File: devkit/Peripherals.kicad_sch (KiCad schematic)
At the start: 46 parts, among them IC501 APDS-9306-065, IC502 BMI270, IC503 LIS2MDLTR, IC504 BMP581, IC505 DRV2603RUNT, IC506 PCA9306JK, IC507 RV-8263-C8, J501 Jumper, J502 Jumper, J503 Jumper, J504 Jumper, J505 Jumper, J506 Jumper, J507 Jumper, M501 Vibrator DC Motor, X501 Current, X502 I2S, X503 Current, X504 I2C, X505 Current, X506 Current, X507 Current, X508 Current, X509 Motor, X510 Current

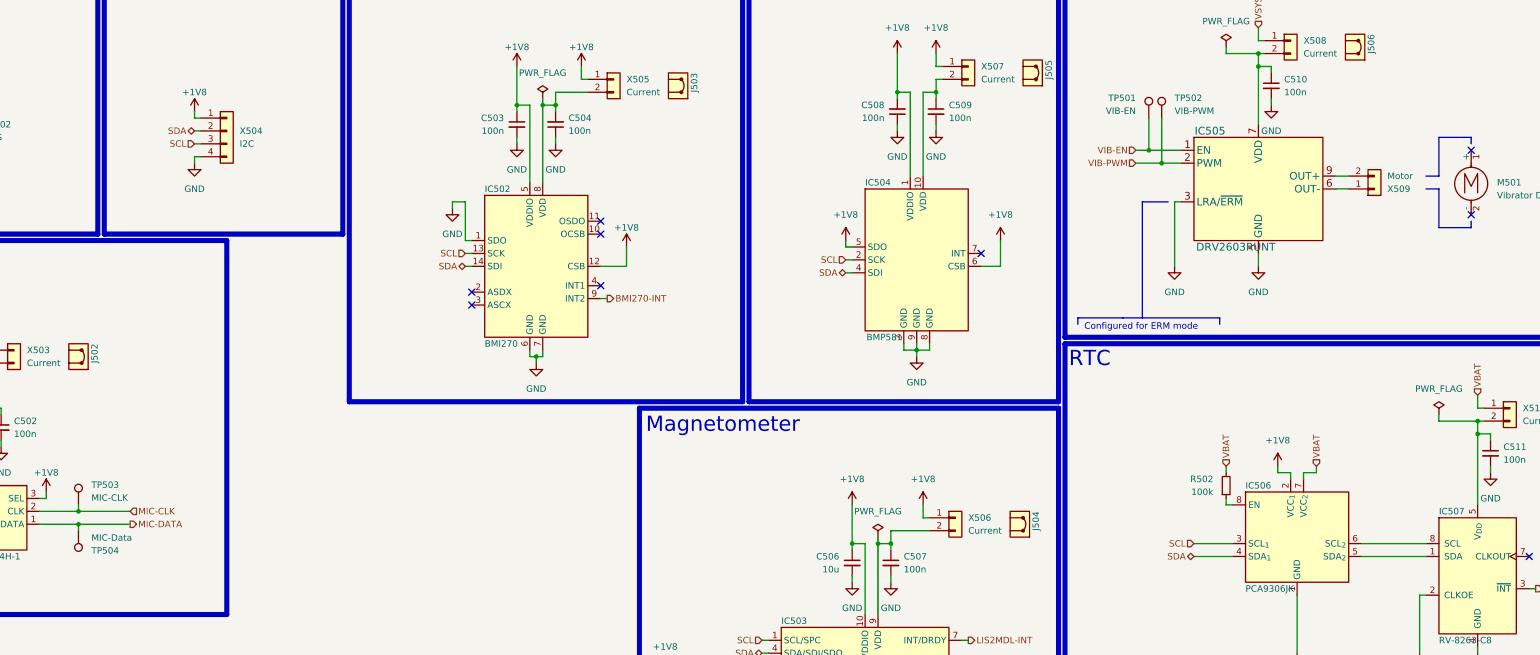
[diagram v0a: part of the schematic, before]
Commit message: Bug: Issue #158
- Fix silkscreens
- Add pull-up resistors to I2C lines
- Set the Pull-Up for Flash CS to NA
- Fix wrong part number for the I2C header

Closes #158

Signed-off-by: Daniel Kampert <DanielKampert@kampis-elektroecke.de>
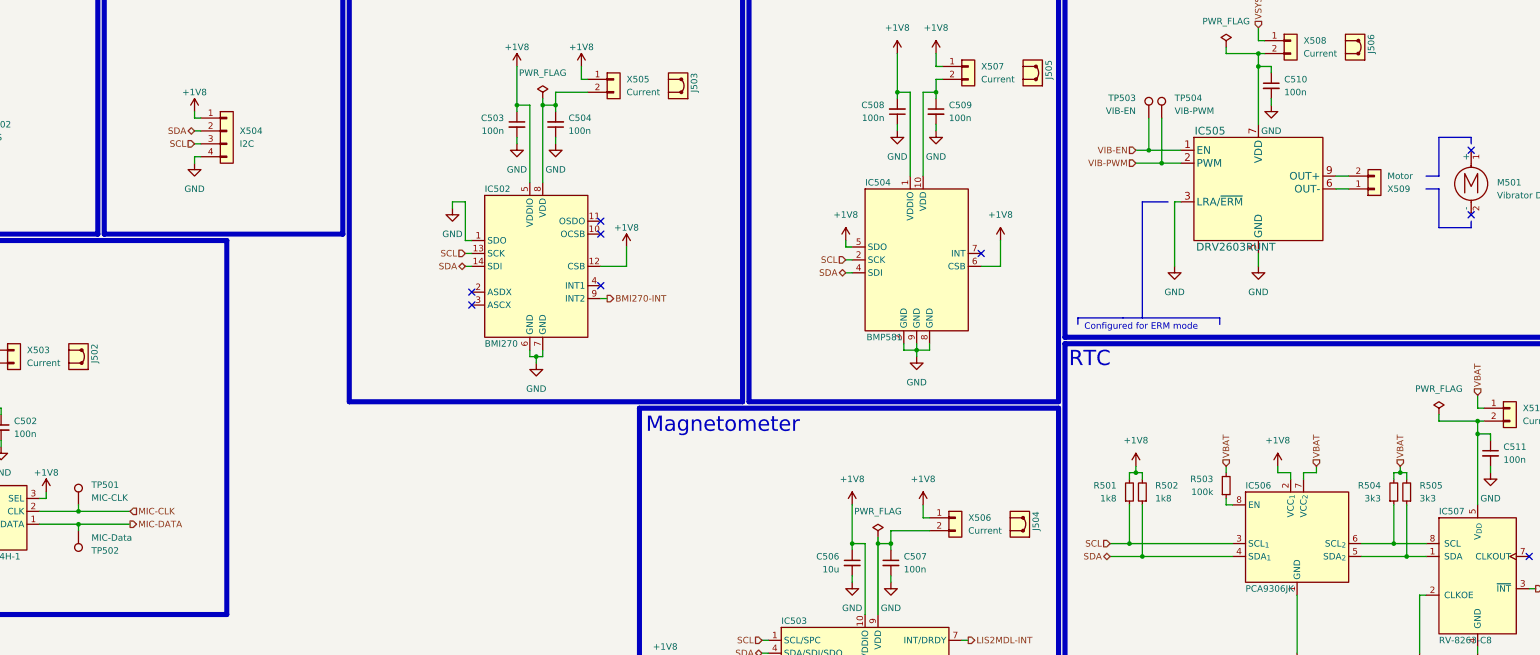
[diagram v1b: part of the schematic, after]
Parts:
- added R501, R502: 1k8, Resistor_SMD:R_0402_1005Metric, symbol Device:R_Small
- added R504, R505: 3k3, Resistor_SMD:R_0402_1005Metric, symbol Device:R_Small
- X504: manf# 77311-818-02LF -> 77311-818-04LF; mouser# 649-77311-818-02LF -> 649-77311-818-04LF
- renumbered R502 to R503, TP503 to TP501, TP504 to TP502, TP501 to TP503, TP502 to TP504
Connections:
- net +1V8: now also R501.2, R502.2
- net SCL: now also R501.1
- net SDA: now also R502.1
- net VBAT: now also R504.2, R505.2
- net at IC506.5 (SDA_{2}), IC507.1 (SDA): now also R505.1
- net at IC506.6 (SCL_{2}), IC507.8 (SCL): now also R504.1

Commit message: Release 1.2.1
Signed-off-by: Daniel Kampert <DanielKampert@kampis-elektroecke.de>
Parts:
- R501, R502: manf# RC0404FR-071K8L -> RC0402FR-071K8L; mouser# 603-RC0404FR-071K8L -> 603-RC0402FR-071K8L
- R503: manf# RC0404FR-07100KL -> RC0402FR-07100KL; mouser# 603-RC0404FR-07100KL -> 603-RC0402FR-07100KL
- R504, R505: manf# RC0404FR-073K3L -> RC0402FR-073K3L; mouser# 603-RC0404FR-073K3L -> 603-RC0402FR-073K3L
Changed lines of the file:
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@@
 			)
 		)
-		(property "manf#" "RC0404FR-073K3L"
+		(property "manf#" "RC0402FR-073K3L"
 			(at 364.49 121.92 0)
 			(effects
@@
 			)
 		)
-		(property "mouser#" "603-RC0404FR-073K3L"
+		(property "mouser#" "603-RC0402FR-073K3L"
 			(at 364.49 121.92 0)
 			(effects
@@
 			)
 		)
-		(property "manf#" "RC0404FR-071K8L"
+		(property "manf#" "RC0402FR-071K8L"
 			(at 314.96 121.92 0)
 			(effects
@@
 			)
 		)
-		(property "mouser#" "603-RC0404FR-071K8L"
+		(property "mouser#" "603-RC0402FR-071K8L"
 			(at 314.96 121.92 0)
 			(effects
@@
 			)
 		)
-		(property "manf#" "RC0404FR-07100KL"
+		(property "manf#" "RC0402FR-07100KL"
 			(at 331.47 120.65 0)
 			(effects
@@
 			)
 		)
-		(property "mouser#" "603-RC0404FR-07100KL"
+		(property "mouser#" "603-RC0402FR-07100KL"
 			(at 331.47 120.65 0)
 			(effects
@@
 			)
 		)
-		(property "manf#" "RC0404FR-073K3L"
+		(property "manf#" "RC0402FR-073K3L"
 			(at 367.03 121.92 0)
 			(effects
@@
 			)
 		)
-		(property "mouser#" "603-RC0404FR-073K3L"
+		(property "mouser#" "603-RC0402FR-073K3L"
 			(at 367.03 121.92 0)
 			(effects
@@
 			)
 		)
-		(property "manf#" "RC0404FR-071K8L"
+		(property "manf#" "RC0402FR-071K8L"
 			(at 312.42 121.92 0)
 			(effects
@@
 			)
 		)
-		(property "mouser#" "603-RC0404FR-071K8L"
+		(property "mouser#" "603-RC0402FR-071K8L"
 			(at 312.42 121.92 0)
 			(effects

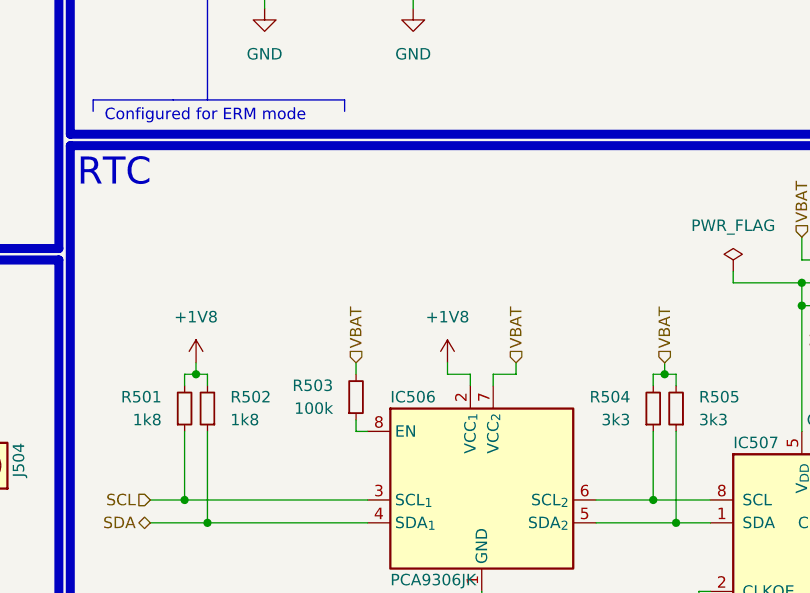
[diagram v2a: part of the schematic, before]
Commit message: Bug: Issue #172
- Fix wrong resistor for VREF2 pin for the level shifter
- Update changelog

Closes #172

Signed-off-by: Daniel Kampert <DanielKampert@kampis-elektroecke.de>
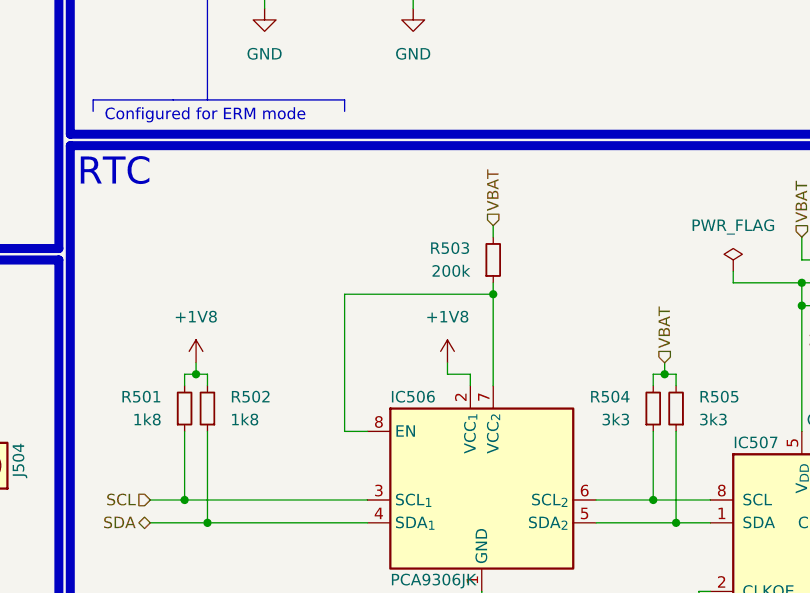
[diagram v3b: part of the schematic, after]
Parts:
- R503: value 100k -> 200k; manf# RC0402FR-07100KL -> RC0402FR-07200KL; mouser# 603-RC0402FR-07100KL -> 603-RC0402FR-07200KL
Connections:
- net VBAT: no longer IC506.7 (VCC_{2})
- net at IC506.8 (EN), R503.1: now also IC506.7 (VCC_{2})
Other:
- moved on the sheet: R503
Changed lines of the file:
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@@
 	)
 	(junction
+		(at 346.71 109.22)
+		(diameter 0)
+		(color 0 0 0 0)
+	)
+	(junction
 		(at 19.05 111.76)
 		(diameter 0)
@@
 	(wire
 		(pts
-			(xy 331.47 123.19) (xy 331.47 124.46)
+			(xy 346.71 107.95) (xy 346.71 109.22)
 		)
 		(stroke
@@
 	(wire
 		(pts
-			(xy 331.47 116.84) (xy 331.47 118.11)
+			(xy 346.71 101.6) (xy 346.71 102.87)
 		)
 		(stroke
@@
 	(wire
 		(pts
-			(xy 349.25 116.84) (xy 349.25 118.11)
-		)
-		(stroke
-			(width 0)
-			(type default)
-		)
-	)
-	(wire
-		(pts
 			(xy 199.39 43.18) (xy 199.39 45.72)
 		)
@@
 	(wire
 		(pts
+			(xy 330.2 109.22) (xy 346.71 109.22)
+		)
+		(stroke
+			(width 0)
+			(type default)
+		)
+	)
+	(wire
+		(pts
 			(xy 196.85 93.98) (xy 196.85 95.25)
 		)
@@
 	(wire
 		(pts
-			(xy 331.47 124.46) (xy 332.74 124.46)
+			(xy 330.2 124.46) (xy 332.74 124.46)
 		)
 		(stroke
@@
 	(wire
 		(pts
-			(xy 346.71 118.11) (xy 346.71 119.38)
+			(xy 346.71 109.22) (xy 346.71 119.38)
 		)
 		(stroke
@@
 	(wire
 		(pts
+			(xy 330.2 109.22) (xy 330.2 124.46)
+		)
+		(stroke
+			(width 0)
+			(type default)
+		)
+	)
+	(wire
+		(pts
 			(xy 313.69 118.11) (xy 313.69 116.84)
 		)
@@
 	(wire
 		(pts
-			(xy 349.25 118.11) (xy 346.71 118.11)
-		)
-		(stroke
-			(width 0)
-			(type default)
-		)
-	)
-	(wire
-		(pts
 			(xy 364.49 132.08) (xy 370.84 132.08)
 		)
@@
 		)
 	)
-	(hierarchical_label "VBAT"
-		(shape input)
-		(at 349.25 116.84 90)
-		(effects
-			(font
-				(size 1.27 1.27)
-			)
-			(justify left)
-		)
-	)
 	(hierarchical_label "SDA"
 		(shape bidirectional)
@@
 	(hierarchical_label "VBAT"
 		(shape input)
-		(at 331.47 116.84 90)
+		(at 346.71 101.6 90)
 		(effects
 			(font
@@
 	(symbol
 		(lib_id "Device:R_Small")
-		(at 331.47 120.65 0)
+		(at 346.71 105.41 0)
 		(mirror x)
 		(unit 1)
@@
 		(fields_autoplaced yes)
 		(property "Reference" "R503"
-			(at 328.93 119.38 0)
+			(at 344.17 104.14 0)
 			(effects
 				(font
@@
 			)
 		)
-		(property "Value" "100k"
-			(at 328.93 121.92 0)
+		(property "Value" "200k"
+			(at 344.17 106.68 0)
 			(effects
 				(font
@@
 		)
 		(property "Footprint" "Resistor_SMD:R_0402_1005Metric"
-			(at 331.47 120.65 0)
+			(at 346.71 105.41 0)
 			(effects
 				(font
@@
 		)
 		(property "Datasheet" "https://www.mouser.com/catalog/specsheets/YAGEO_PYu_RC_Group_51_RoHS_L_12.pdf"
-			(at 331.47 120.65 0)
+			(at 346.71 105.41 0)
 			(effects
 				(font
@@
 		)
 		(property "Description" "Resistor, small symbol"
-			(at 331.47 120.65 0)
+			(at 346.71 105.41 0)
 			(effects
 				(font
@@
 		)
 		(property "CONFIG" ""
-			(at 331.47 120.65 0)
+			(at 346.71 105.41 0)
 			(effects
 				(font
@@
 		)
 		(property "manf" "YAGEO"
-			(at 331.47 120.65 0)
+			(at 346.71 105.41 0)
 			(effects
 				(font
@@
 			)
 		)
-		(property "manf#" "RC0402FR-07100KL"
-			(at 331.47 120.65 0)
+		(property "manf#" "RC0402FR-07200KL"
+			(at 346.71 105.41 0)
 			(effects
 				(font
@@
 			)
 		)
-		(property "mouser#" "603-RC0402FR-07100KL"
-			(at 331.47 120.65 0)
+		(property "mouser#" "603-RC0402FR-07200KL"
+			(at 346.71 105.41 0)
 			(effects
 				(font

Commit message: Revert "Bug: Issue #172"
This reverts commit d2b21792fba04b32ee89f1631bab4de80096e44a.
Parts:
- R503: value 200k -> 100k; manf# RC0402FR-07200KL -> RC0402FR-07100KL; mouser# 603-RC0402FR-07200KL -> 603-RC0402FR-07100KL
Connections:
- net VBAT: now also IC506.7 (VCC_{2})
- net at IC506.8 (EN), R503.1: no longer IC506.7 (VCC_{2})
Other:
- moved on the sheet: R503
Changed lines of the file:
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@@
 	)
 	(junction
-		(at 346.71 109.22)
-		(diameter 0)
-		(color 0 0 0 0)
-	)
-	(junction
 		(at 19.05 111.76)
 		(diameter 0)
@@
 	(wire
 		(pts
-			(xy 346.71 107.95) (xy 346.71 109.22)
+			(xy 331.47 123.19) (xy 331.47 124.46)
 		)
 		(stroke
@@
 	(wire
 		(pts
-			(xy 346.71 101.6) (xy 346.71 102.87)
+			(xy 331.47 116.84) (xy 331.47 118.11)
 		)
 		(stroke
@@
 	(wire
 		(pts
+			(xy 349.25 116.84) (xy 349.25 118.11)
+		)
+		(stroke
+			(width 0)
+			(type default)
+		)
+	)
+	(wire
+		(pts
 			(xy 199.39 43.18) (xy 199.39 45.72)
 		)
@@
 	(wire
 		(pts
-			(xy 330.2 109.22) (xy 346.71 109.22)
-		)
-		(stroke
-			(width 0)
-			(type default)
-		)
-	)
-	(wire
-		(pts
 			(xy 196.85 93.98) (xy 196.85 95.25)
 		)
@@
 	(wire
 		(pts
-			(xy 330.2 124.46) (xy 332.74 124.46)
+			(xy 331.47 124.46) (xy 332.74 124.46)
 		)
 		(stroke
@@
 	(wire
 		(pts
-			(xy 346.71 109.22) (xy 346.71 119.38)
+			(xy 346.71 118.11) (xy 346.71 119.38)
 		)
 		(stroke
@@
 	(wire
 		(pts
-			(xy 330.2 109.22) (xy 330.2 124.46)
-		)
-		(stroke
-			(width 0)
-			(type default)
-		)
-	)
-	(wire
-		(pts
 			(xy 313.69 118.11) (xy 313.69 116.84)
 		)
@@
 	(wire
 		(pts
+			(xy 349.25 118.11) (xy 346.71 118.11)
+		)
+		(stroke
+			(width 0)
+			(type default)
+		)
+	)
+	(wire
+		(pts
 			(xy 364.49 132.08) (xy 370.84 132.08)
 		)
@@
 		)
 	)
+	(hierarchical_label "VBAT"
+		(shape input)
+		(at 349.25 116.84 90)
+		(effects
+			(font
+				(size 1.27 1.27)
+			)
+			(justify left)
+		)
+	)
 	(hierarchical_label "SDA"
 		(shape bidirectional)
@@
 	(hierarchical_label "VBAT"
 		(shape input)
-		(at 346.71 101.6 90)
+		(at 331.47 116.84 90)
 		(effects
 			(font
@@
 	(symbol
 		(lib_id "Device:R_Small")
-		(at 346.71 105.41 0)
+		(at 331.47 120.65 0)
 		(mirror x)
 		(unit 1)
@@
 		(fields_autoplaced yes)
 		(property "Reference" "R503"
-			(at 344.17 104.14 0)
+			(at 328.93 119.38 0)
 			(effects
 				(font
@@
 			)
 		)
-		(property "Value" "200k"
-			(at 344.17 106.68 0)
+		(property "Value" "100k"
+			(at 328.93 121.92 0)
 			(effects
 				(font
@@
 		)
 		(property "Footprint" "Resistor_SMD:R_0402_1005Metric"
-			(at 346.71 105.41 0)
+			(at 331.47 120.65 0)
 			(effects
 				(font
@@
 		)
 		(property "Datasheet" "https://www.mouser.com/catalog/specsheets/YAGEO_PYu_RC_Group_51_RoHS_L_12.pdf"
-			(at 346.71 105.41 0)
+			(at 331.47 120.65 0)
 			(effects
 				(font
@@
 		)
 		(property "Description" "Resistor, small symbol"
-			(at 346.71 105.41 0)
+			(at 331.47 120.65 0)
 			(effects
 				(font
@@
 		)
 		(property "CONFIG" ""
-			(at 346.71 105.41 0)
+			(at 331.47 120.65 0)
 			(effects
 				(font
@@
 		)
 		(property "manf" "YAGEO"
-			(at 346.71 105.41 0)
+			(at 331.47 120.65 0)
 			(effects
 				(font
@@
 			)
 		)
-		(property "manf#" "RC0402FR-07200KL"
-			(at 346.71 105.41 0)
+		(property "manf#" "RC0402FR-07100KL"
+			(at 331.47 120.65 0)
 			(effects
 				(font
@@
 			)
 		)
-		(property "mouser#" "603-RC0402FR-07200KL"
-			(at 346.71 105.41 0)
+		(property "mouser#" "603-RC0402FR-07100KL"
+			(at 331.47 120.65 0)
 			(effects
 				(font
